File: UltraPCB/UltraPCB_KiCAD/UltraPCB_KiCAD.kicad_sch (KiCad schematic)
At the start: 45 parts, among them J1 USB_C_Receptacle_PowerOnly_6P, J2 Conn_01x04_Pin, Q1 SQ2325ES-T1_GE3, Q2 SQ2325ES-T1_GE3, Q3 SQ2325ES-T1_GE3, Q4 SQ2325ES-T1_GE3, Q5 SQ2325ES-T1_GE3, Q6 IRLML6244, SW1 SW_Push, SW2 SW_Push, U2 LM3670MF-3.3, U3 LTC-4627JD, U4 STM32F030K6Tx

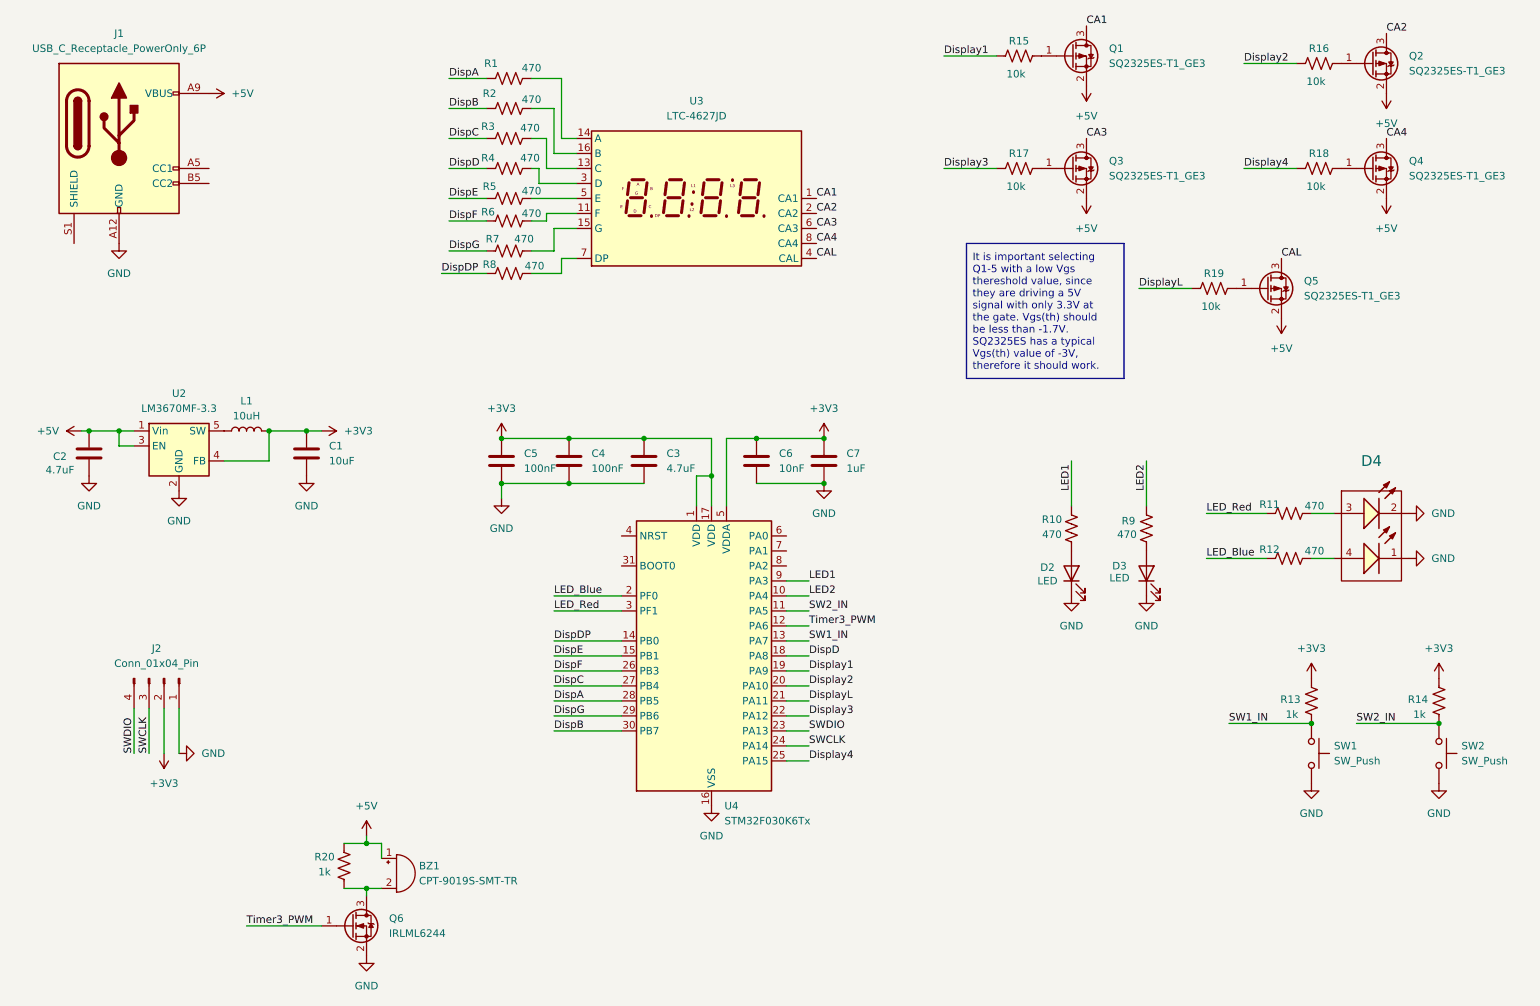
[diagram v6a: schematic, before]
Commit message: Changed to KiCAD 9 and rounded all tracks
Plugin Round Tracks was used for automatically rounding all tracks
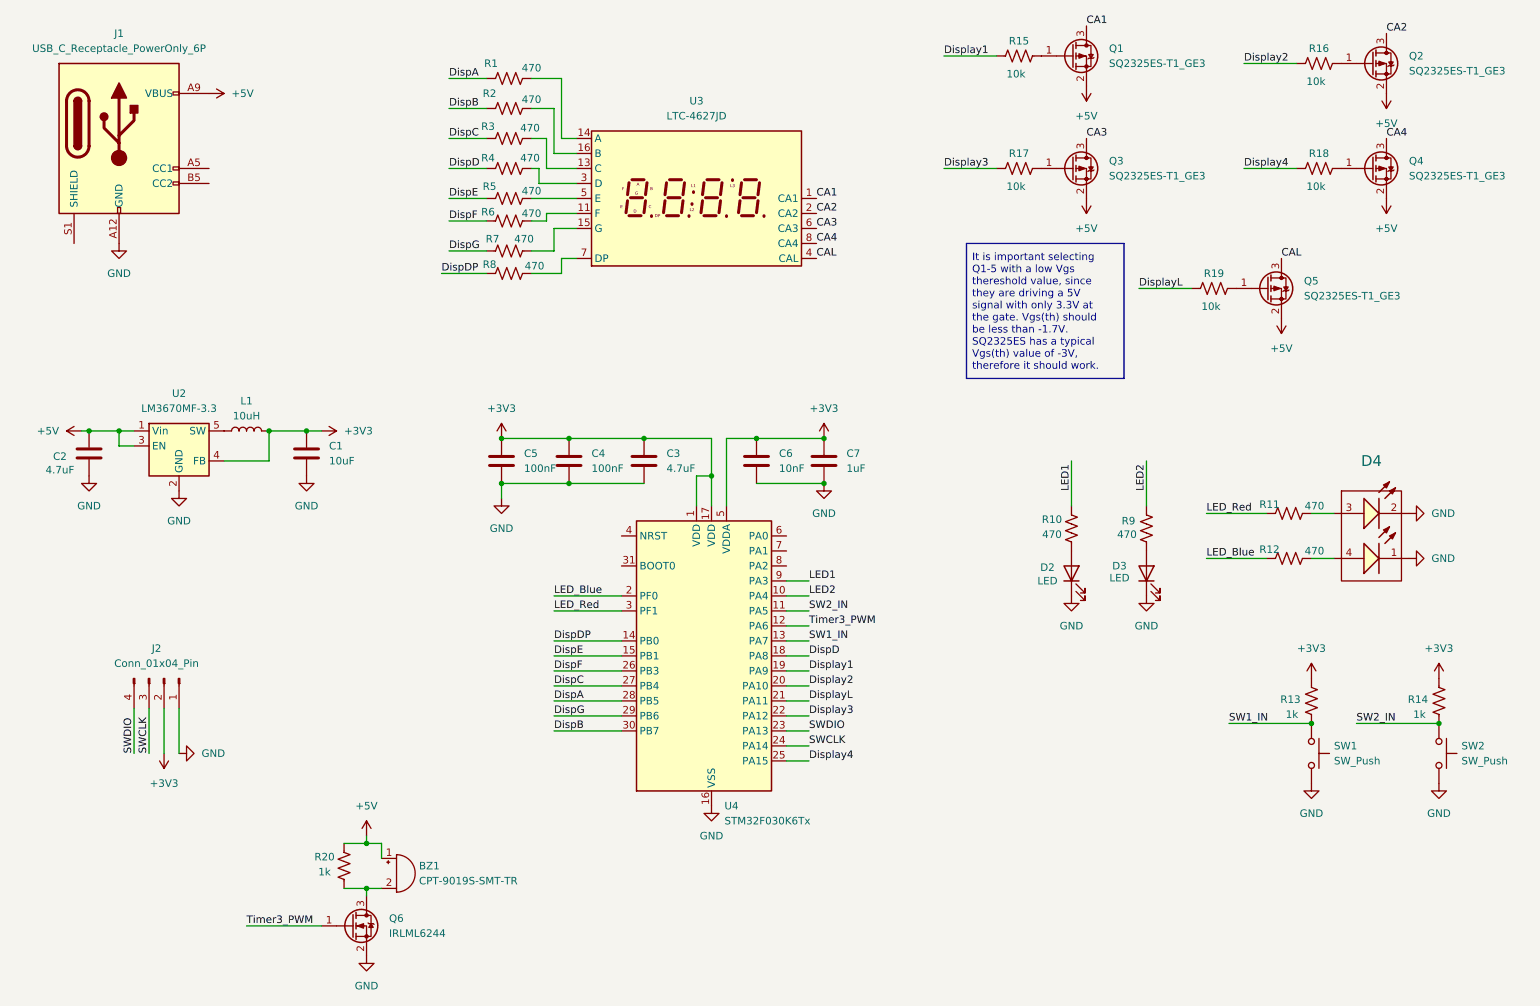
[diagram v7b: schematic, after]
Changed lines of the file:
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@@
 (kicad_sch
-	(version 20231120)
+	(version 20250114)
 	(generator "eeschema")
-	(generator_version "8.0")
+	(generator_version "9.0")
 	(paper "A4")
 	(title_block
@@
 		(comment 2 "All units in mm")
 	)
+	(text_box "It is important selecting Q1-5 with a low Vgs thereshold value, since they are driving a 5V signal with only 3.3V at the gate. Vgs(th) should be less than -1.7V. SQ2325ES has a typical Vgs(th) value of -3V, therefore it should work."
+		(exclude_from_sim no)
+		(at 181.61 60.96 0)
+		(size 26.67 22.86)
+		(margins 0.9525 0.9525 0.9525 0.9525)
+		(stroke
+			(width 0)
+			(type default)
+		)
+		(fill
+			(type none)
+		)
+		(effects
+			(font
+				(size 1.27 1.27)
+			)
+			(justify left)
+		)
+	)
 	(junction
 		(at 114.3 93.98)
@@
 		)
 	)
-	(text_box "It is important selecting Q1-5 with a low Vgs thereshold value, since they are driving a 5V signal with only 3.3V at the gate. Vgs(th) should be less than -1.7V. SQ2325ES has a typical Vgs(th) value of -3V, therefore it should work."
-		(exclude_from_sim no)
-		(at 181.61 60.96 0)
-		(size 26.67 22.86)
-		(stroke
-			(width 0)
-			(type default)
-		)
-		(fill
-			(type none)
-		)
-		(effects
-			(font
-				(size 1.27 1.27)
-			)
-			(justify left)
-		)
-	)
 	(label "SWCLK"
 		(at 154.94 146.05 0)
@@
 		)
 	)
+	(embedded_fonts no)
 )

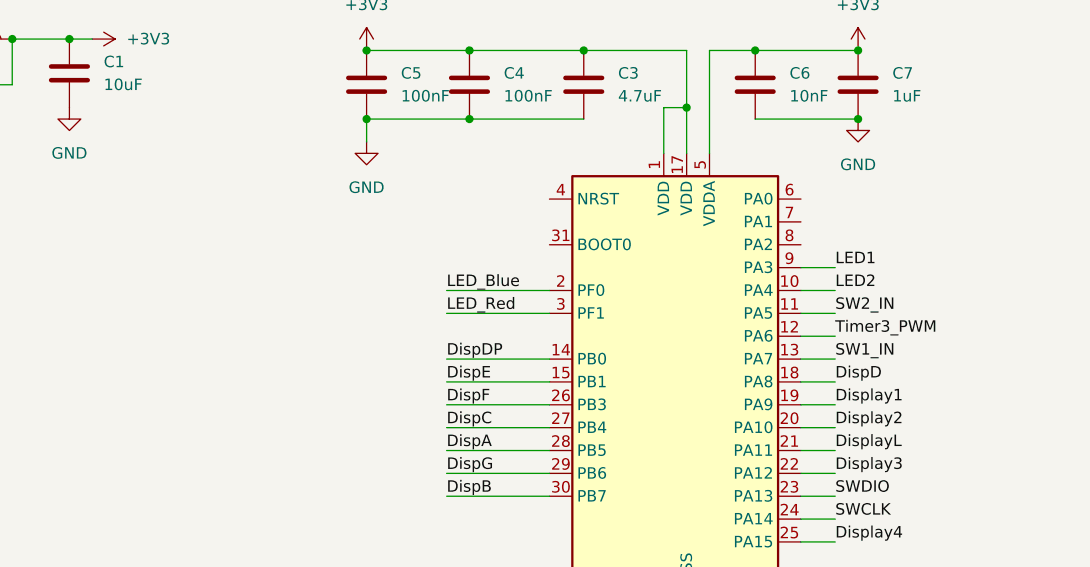
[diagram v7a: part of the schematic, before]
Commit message: Added quartz
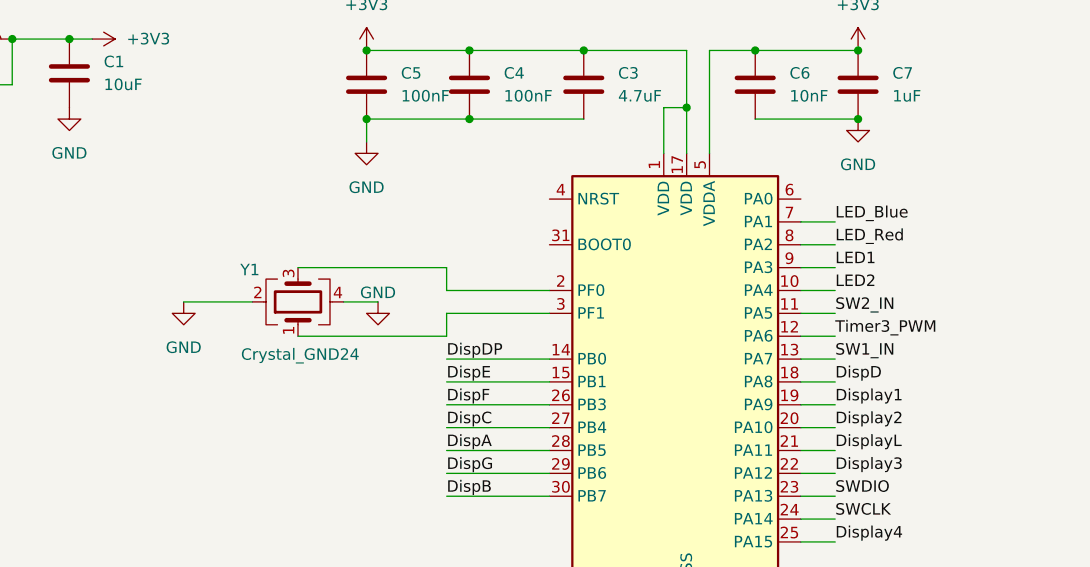
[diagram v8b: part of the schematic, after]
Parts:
- added Y1: Crystal_GND24, Crystal:Crystal_SMD_3225-4Pin_3.2x2.5mm, symbol Device:Crystal_GND24
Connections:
- net GND: now also Y1.2, Y1.4
- net LED_Blue: now also U4.7 (PA1); no longer U4.2 (PF0)
- net LED_Red: now also U4.8 (PA2); no longer U4.3 (PF1)
- new net: U4.2 (PF0), Y1.3
- new net: U4.3 (PF1), Y1.1
